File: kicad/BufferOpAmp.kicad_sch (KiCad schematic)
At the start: 4 parts, among them U1 TL072

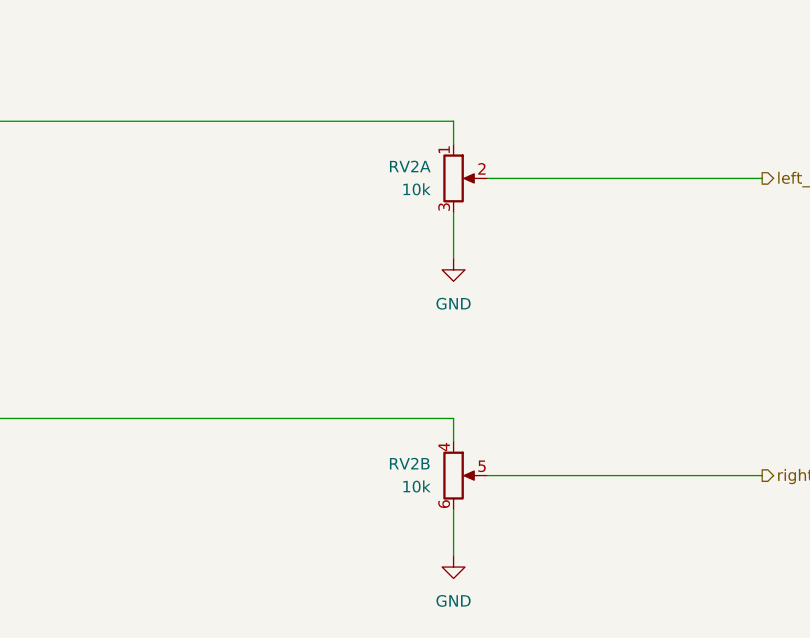
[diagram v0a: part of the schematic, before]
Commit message: main schematic done, layout started
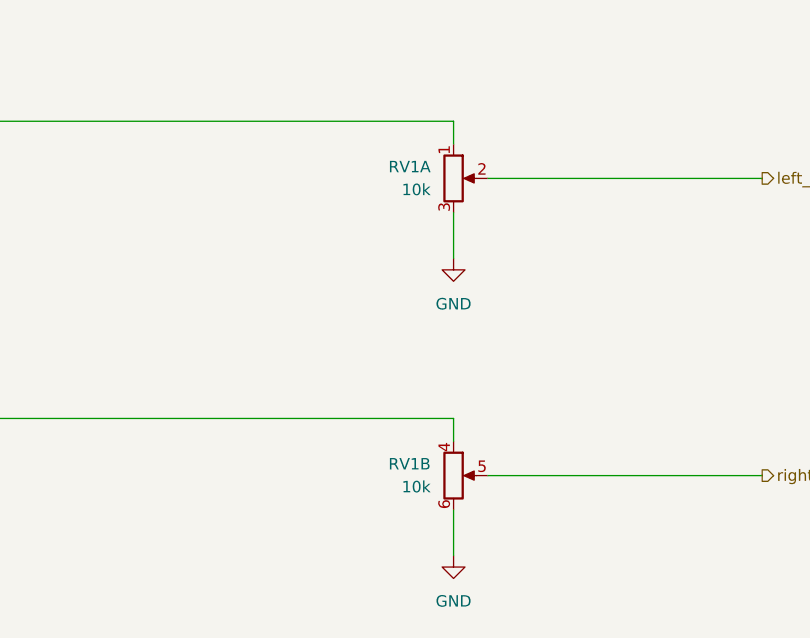
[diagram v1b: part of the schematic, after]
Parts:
- renumbered RV2 to RV1
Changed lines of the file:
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@@
   (symbol (lib_id "Device:R_Potentiometer_Dual_Separate") (at 166.37 52.07 0) (unit 1)
     (in_bom yes) (on_board yes) (dnp no) (fields_autoplaced)
-    (property "Reference" "RV2" (at 163.83 50.8 0)
+    (property "Reference" "RV1" (at 163.83 50.8 0)
       (effects (font (size 1.27 1.27)) (justify right))
     )
@@
       (project "Tiny4xPoweredStereoMixer"
         (path "/68c4b081-ef47-4ba5-a55f-4ef66cb2b598/f21b05ca-c53e-4c9f-92f9-42535cdfa7f7"
+          (reference "RV1") (unit 1)
+        )
+        (path "/68c4b081-ef47-4ba5-a55f-4ef66cb2b598/552f3912-3928-454a-823e-6f183577fda8"
           (reference "RV2") (unit 1)
-        )
-        (path "/68c4b081-ef47-4ba5-a55f-4ef66cb2b598/552f3912-3928-454a-823e-6f183577fda8"
-          (reference "RV1") (unit 1)
         )
         (path "/68c4b081-ef47-4ba5-a55f-4ef66cb2b598/4f5d350b-a08e-4f50-b16f-b5f92c91b503"
@@
   (symbol (lib_id "Device:R_Potentiometer_Dual_Separate") (at 166.37 85.09 0) (unit 2)
     (in_bom yes) (on_board yes) (dnp no) (fields_autoplaced)
-    (property "Reference" "RV2" (at 163.83 83.82 0)
+    (property "Reference" "RV1" (at 163.83 83.82 0)
       (effects (font (size 1.27 1.27)) (justify right))
     )
@@
       (project "Tiny4xPoweredStereoMixer"
         (path "/68c4b081-ef47-4ba5-a55f-4ef66cb2b598/f21b05ca-c53e-4c9f-92f9-42535cdfa7f7"
+          (reference "RV1") (unit 2)
+        )
+        (path "/68c4b081-ef47-4ba5-a55f-4ef66cb2b598/552f3912-3928-454a-823e-6f183577fda8"
           (reference "RV2") (unit 2)
         )
-        (path "/68c4b081-ef47-4ba5-a55f-4ef66cb2b598/552f3912-3928-454a-823e-6f183577fda8"
-          (reference "RV1") (unit 2)
-        )
-        (path "/68c4b081-ef47-4ba5-a55f-4ef66cb2b598/4f5d350b-a08e-4f50-b16f-b5f92c91b503"
+        (path "/68c4b081-ef47-4ba5-a55f-4ef66cb2b598/4f5d350b-a08e-4f50-b16f-b5f92c91b503"

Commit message: completed reva layout
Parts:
- C7, C8: Mouser (none) -> 791-0603B104J250CT
- RV1: footprint Potentiometer_THT:Potentiometer_Alps_RK09L_Double_Horizontal -> Potentiometers:Potentiometer_Alps_RK09L_Double_Horizontal
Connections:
- net left_channel_buffered: now also RV1.5; no longer RV1.2
- net right_channel_buffered: now also RV1.2; no longer RV1.5
- net at U1.6 (-), U1.7: now also RV1.1; no longer RV1.4
- net at U1.1, U1.2 (-): now also RV1.4; no longer RV1.1
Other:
- moved on the sheet: RV1A, RV1B
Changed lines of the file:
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@@
     )
   )
-  (symbol (lib_id "Device:R_Potentiometer_Dual_Separate") (at 166.37 52.07 0) (unit 1)
-    (in_bom yes) (on_board yes) (dnp no) (fields_autoplaced)
-    (property "Reference" "RV1" (at 163.83 50.8 0)
-      (effects (font (size 1.27 1.27)) (justify right))
-    )
-    (property "Value" "10k" (at 163.83 53.34 0)
-      (effects (font (size 1.27 1.27)) (justify right))
-    )
-    (property "Footprint" "Potentiometer_THT:Potentiometer_Alps_RK09L_Double_Horizontal" (at 166.37 52.07 0)
-      (effects (font (size 1.27 1.27)) hide)
-    )
-    (property "Datasheet" "https://tech.alpsalpine.com/e/products/detail/RK09L12B0A4S" (at 166.37 52.07 0)
-      (effects (font (size 1.27 1.27)) hide)
-    )
-    (property "Mouser" "688-RK09L12B0A4S " (at 166.37 52.07 0)
+  (symbol (lib_id "Device:R_Potentiometer_Dual_Separate") (at 166.37 85.09 0) (unit 1)
+    (in_bom yes) (on_board yes) (dnp no) (fields_autoplaced)
+    (property "Reference" "RV1" (at 163.83 83.82 0)
+      (effects (font (size 1.27 1.27)) (justify right))
+    )
+    (property "Value" "10k" (at 163.83 86.36 0)
+      (effects (font (size 1.27 1.27)) (justify right))
+    )
+    (property "Footprint" "Potentiometers:Potentiometer_Alps_RK09L_Double_Horizontal" (at 166.37 85.09 0)
+      (effects (font (size 1.27 1.27)) hide)
+    )
+    (property "Datasheet" "https://tech.alpsalpine.com/e/products/detail/RK09L12B0A4S" (at 166.37 85.09 0)
+      (effects (font (size 1.27 1.27)) hide)
+    )
+    (property "Mouser" "688-RK09L12B0A4S " (at 166.37 85.09 0)
       (effects (font (size 1.27 1.27)) hide)
     )
@@
       (effects (font (size 1.27 1.27)) hide)
     )
-    (property "Mouser" "" (at 111.76 160.02 0)
+    (property "Mouser" "791-0603B104J250CT" (at 111.76 160.02 0)
       (effects (font (size 1.27 1.27)) hide)
     )
@@
       (effects (font (size 1.27 1.27)) hide)
     )
-    (property "Mouser" "" (at 99.06 160.02 0)
+    (property "Mouser" "791-0603B104J250CT" (at 99.06 160.02 0)
       (effects (font (size 1.27 1.27)) hide)
     )
@@
     )
   )
-  (symbol (lib_id "Device:R_Potentiometer_Dual_Separate") (at 166.37 85.09 0) (unit 2)
-    (in_bom yes) (on_board yes) (dnp no) (fields_autoplaced)
-    (property "Reference" "RV1" (at 163.83 83.82 0)
-      (effects (font (size 1.27 1.27)) (justify right))
-    )
-    (property "Value" "10k" (at 163.83 86.36 0)
-      (effects (font (size 1.27 1.27)) (justify right))
-    )
-    (property "Footprint" "Potentiometer_THT:Potentiometer_Alps_RK09L_Double_Horizontal" (at 166.37 85.09 0)
-      (effects (font (size 1.27 1.27)) hide)
-    )
-    (property "Datasheet" "https://tech.alpsalpine.com/e/products/detail/RK09L12B0A4S" (at 166.37 85.09 0)
-      (effects (font (size 1.27 1.27)) hide)
-    )
-    (property "Mouser" "688-RK09L12B0A4S " (at 166.37 85.09 0)
-      (effects (font (size 1.27 1.27)) hide)
-    )
+  (symbol (lib_id "Device:R_Potentiometer_Dual_Separate") (at 166.37 52.07 0) (unit 2)
+    (in_bom yes) (on_board yes) (dnp no) (fields_autoplaced)
+    (property "Reference" "RV1" (at 163.83 50.8 0)
+      (effects (font (size 1.27 1.27)) (justify right))
+    )
+    (property "Value" "10k" (at 163.83 53.34 0)
+      (effects (font (size 1.27 1.27)) (justify right))
+    )
+    (property "Footprint" "Potentiometers:Potentiometer_Alps_RK09L_Double_Horizontal" (at 166.37 52.07 0)
+      (effects (font (size 1.27 1.27)) hide)
+    )
+    (property "Datasheet" "https://tech.alpsalpine.com/e/products/detail/RK09L12B0A4S" (at 166.37 52.07 0)
+      (effects (font (size 1.27 1.27)) hide)
+    )
+    (property "Mouser" "688-RK09L12B0A4S " (at 166.37 52.07 0)
+      (effects (font (size 1.27 1.27)) hide)
+    )

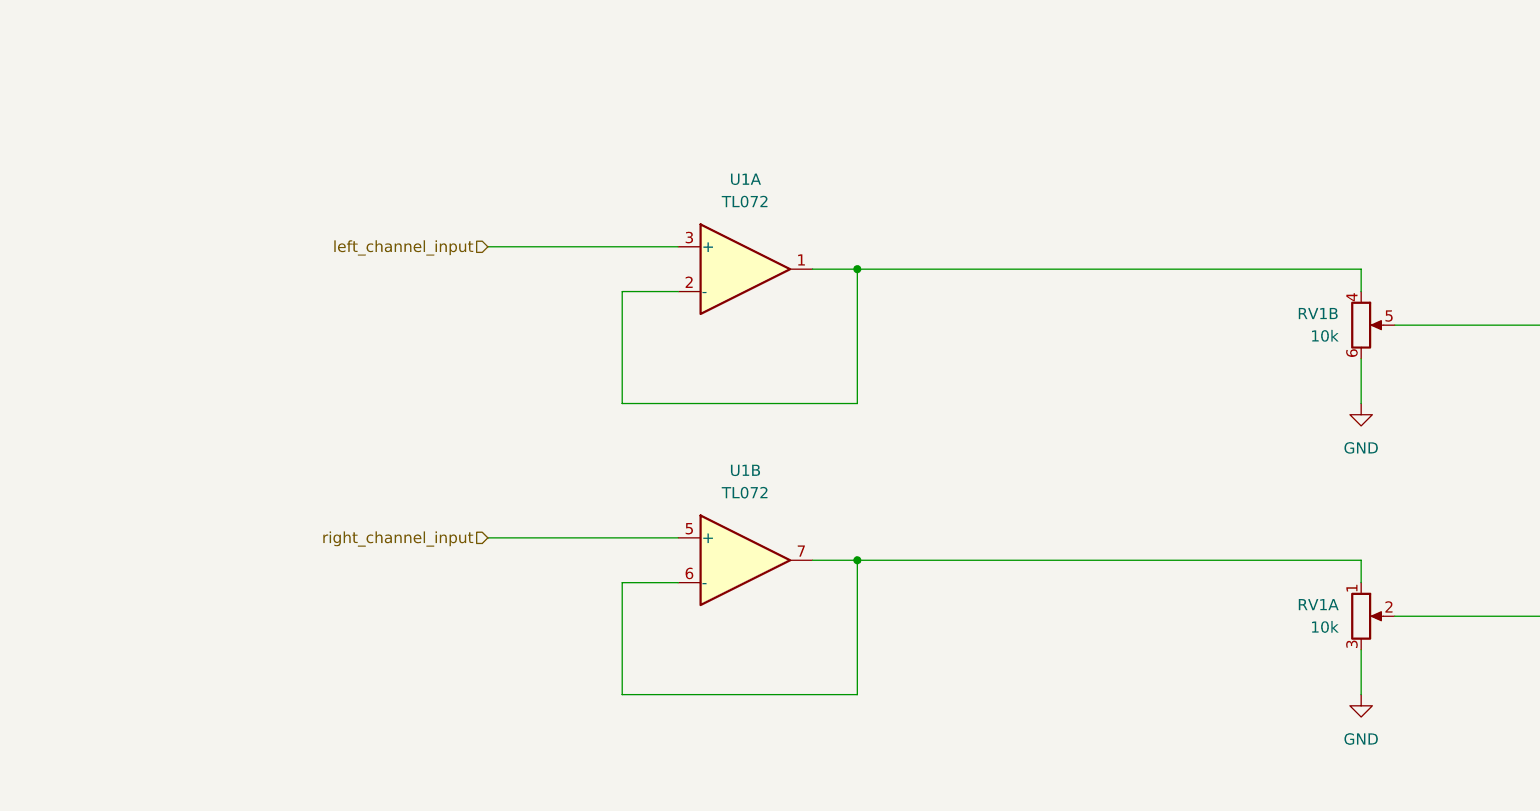
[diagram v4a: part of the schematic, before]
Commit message: -  Fixed in-rush current problem using soft-start design. https://github.com/cracked-machine/Tiny4xPoweredStereoMixer/issues/4 - Fixed reversed pots. https://github.com/cracked-machine/Tiny4xPoweredStereoMixer/issues/3 - Made more space surrounding pwr in connector. https://github.com/cracked-machine/Tiny4xPoweredStereoMixer/issues/8
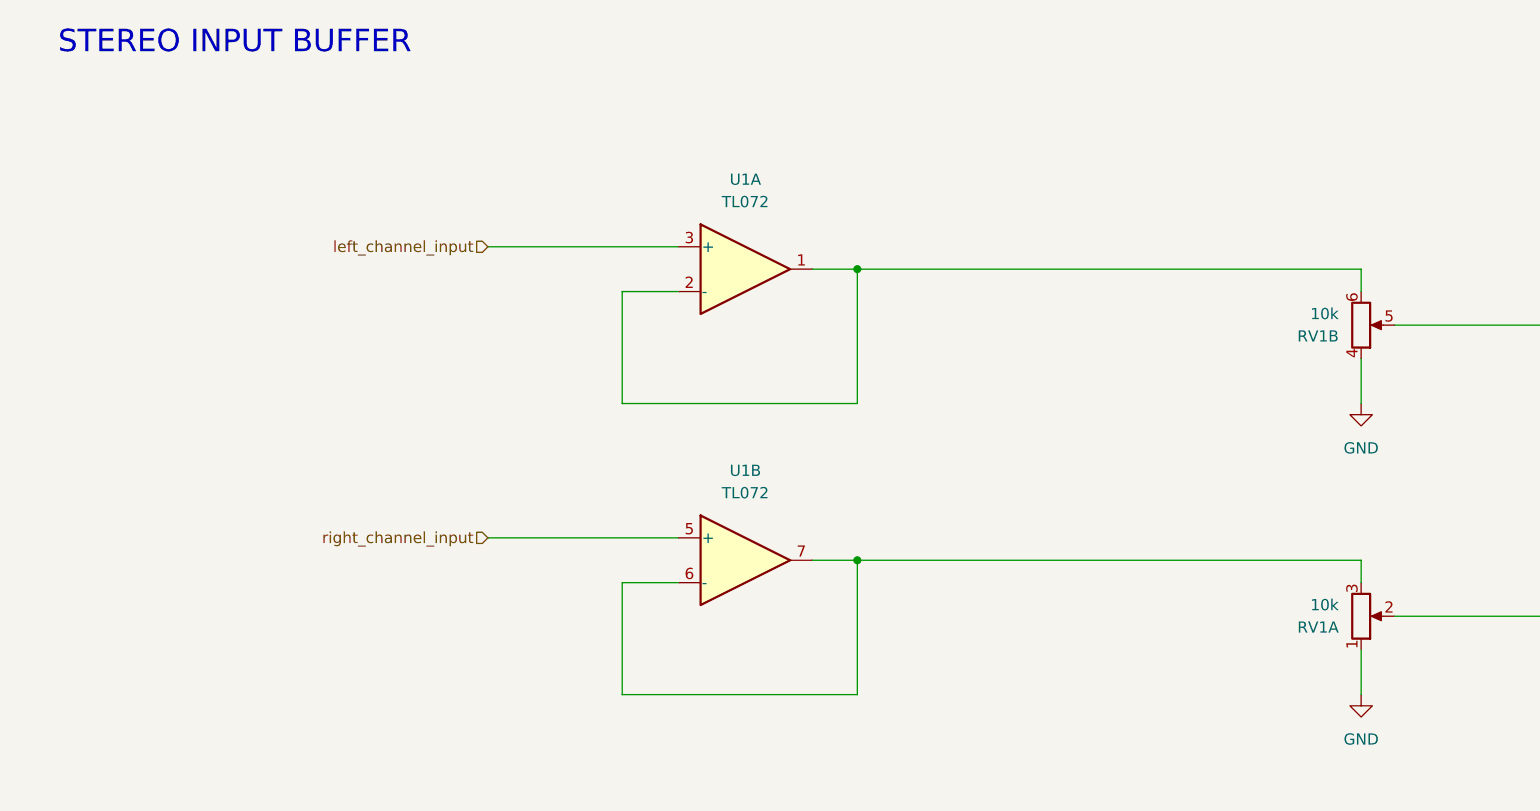
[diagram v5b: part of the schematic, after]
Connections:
- net GND: now also RV1.1, RV1.4; no longer RV1.3, RV1.6
- net at U1.6 (-), U1.7: now also RV1.3; no longer RV1.1
- net at U1.1, U1.2 (-): now also RV1.6; no longer RV1.4
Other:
- note added: "STEREO INPUT BUFFER"
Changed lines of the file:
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@@
 	(generator_version "8.0")
 	(paper "A4")
+	(title_block
+		(rev "B")
+	)
 	(junction
 		(at 105.41 170.18)
@@
 			(width 0)
 			(type default)
+		)
+	)
+	(text "STEREO INPUT BUFFER"
+		(exclude_from_sim no)
+		(at 38.608 20.066 0)
+		(effects
+			(font
+				(size 2.54 2.54)
+			)
 		)
 	)
@@
 			)
 		)
-		(property "Description" ""
+		(property "Description" "Dual Low-Noise JFET-Input Operational Amplifiers, DIP-8/SOIC-8"
 			(at 147.32 161.29 0)
 			(effects
@@
 			)
 		)
-		(property "Description" ""
+		(property "Description" "Dual Low-Noise JFET-Input Operational Amplifiers, DIP-8/SOIC-8"
 			(at 96.52 78.74 0)
 			(effects
@@
 			)
 		)
-		(property "Description" ""
+		(property "Description" "Power symbol creates a global label with name \"+12V\""
 			(at 99.06 149.86 0)
 			(effects
@@
 			)
 		)
-		(property "Description" ""
+		(property "Description" "Power symbol creates a global label with name \"-12V\""
 			(at 111.76 149.86 0)
 			(effects
@@
 			)
 		)
-		(property "Description" ""
+		(property "Description" "Power symbol creates a global label with name \"+12V\""
 			(at 144.78 148.59 0)
 			(effects
@@
 			)
 		)
-		(property "Description" ""
+		(property "Description" "Power symbol creates a global label with name \"GND\" , ground"
 			(at 105.41 175.26 0)
 			(effects
@@
 		(lib_id "Device:R_Potentiometer_Dual_Separate")
 		(at 166.37 85.09 0)
+		(mirror x)
 		(unit 1)
 		(exclude_from_sim no)
@@
 		(on_board yes)
 		(dnp no)
-		(fields_autoplaced yes)
 		(property "Reference" "RV1"
+			(at 163.83 86.36 0)
+			(effects
+				(font
+					(size 1.27 1.27)
+				)
+				(justify right)
+			)
+		)
+		(property "Value" "10k"
 			(at 163.83 83.82 0)
-			(effects
-				(font
-					(size 1.27 1.27)
-				)
-				(justify right)
-			)
-		)
-		(property "Value" "10k"
-			(at 163.83 86.36 0)
 			(effects
 				(font
@@
 			)
 		)
-		(property "Datasheet" "https://tech.alpsalpine.com/e/products/detail/RK09L12B0A4S"
+		(property "Datasheet" "~"
 			(at 166.37 85.09 0)
 			(effects
@@
 			)
 		)
-		(property "Description" ""
+		(property "Description" "Dual potentiometer, separate units"
 			(at 166.37 85.09 0)
 			(effects
@@
 			)
 		)
-		(property "Description" ""
+		(property "Description" "Dual Low-Noise JFET-Input Operational Amplifiers, DIP-8/SOIC-8"
 			(at 96.52 45.72 0)
 			(effects
@@
 			)
 		)
-		(property "Description" ""
+		(property "Description" "Power symbol creates a global label with name \"GND\" , ground"
 			(at 166.37 93.98 0)
 			(effects
@@
 			)
 		)
-		(property "Description" ""
+		(property "Description" "Power symbol creates a global label with name \"GND\" , ground"
 			(at 166.37 60.96 0)
 			(effects
@@
 			)
 		)
-		(property "Datasheet" "https://datasheet.lcsc.com/lcsc/2304140030_Samsung-Electro-Mechanics-CL10B104KA8NNNC_C1590.pdf"
+		(property "Datasheet" "~"
 			(at 111.76 160.02 0)
 			(effects
@@
 			)
 		)
-		(property "Description" ""
+		(property "Description" "Unpolarized capacitor"
 			(at 111.76 160.02 0)
 			(effects
@@
 			)
 		)
-		(property "Datasheet" "https://datasheet.lcsc.com/lcsc/2304140030_Samsung-Electro-Mechanics-CL10B104KA8NNNC_C1590.pdf"
+		(property "Datasheet" "~"
 			(at 99.06 160.02 0)
 			(effects
@@
 			)
 		)
-		(property "Description" ""
+		(property "Description" "Unpolarized capacitor"
 			(at 99.06 160.02 0)
 			(effects
@@
 			)
 		)
-		(property "Description" ""
+		(property "Description" "Power symbol creates a global label with name \"-12V\""
 			(at 144.78 177.8 0)
 			(effects
@@
 		(lib_id "Device:R_Potentiometer_Dual_Separate")
 		(at 166.37 52.07 0)
+		(mirror x)
 		(unit 2)
 		(exclude_from_sim no)
@@
 		(on_board yes)
 		(dnp no)
-		(fields_autoplaced yes)
 		(property "Reference" "RV1"
+			(at 163.83 53.34 0)
+			(effects
+				(font
+					(size 1.27 1.27)
+				)
+				(justify right)
+			)
+		)
+		(property "Value" "10k"
 			(at 163.83 50.8 0)
-			(effects
-				(font
-					(size 1.27 1.27)
-				)
-				(justify right)
-			)
-		)
-		(property "Value" "10k"
-			(at 163.83 53.34 0)
 			(effects
 				(font
@@
 			)
 		)
-		(property "Datasheet" "https://tech.alpsalpine.com/e/products/detail/RK09L12B0A4S"
+		(property "Datasheet" "~"
 			(at 166.37 52.07 0)
 			(effects
@@
 			)
 		)
-		(property "Description" ""
+		(property "Description" "Dual potentiometer, separate units"
 			(at 166.37 52.07 0)
 			(effects
